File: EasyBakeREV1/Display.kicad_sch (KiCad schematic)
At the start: 20 parts, among them U4 SQ2310ES_SOT23, U5 NHD-C12832A1Z

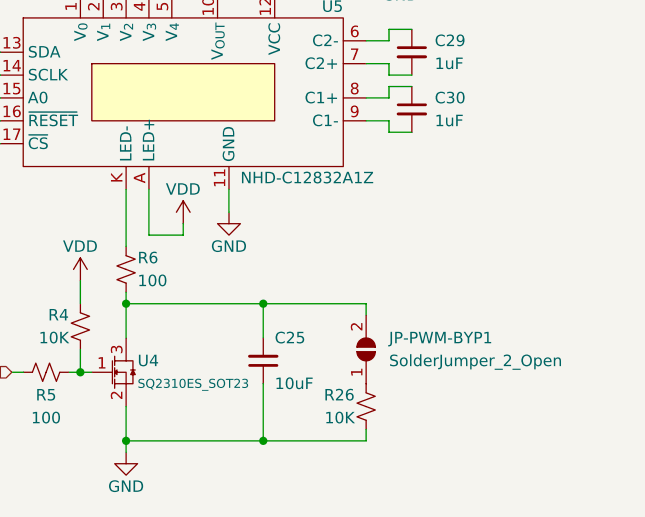
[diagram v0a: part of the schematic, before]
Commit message: REV3 - Reorganize MC pinouts and add LED driver (WIP)
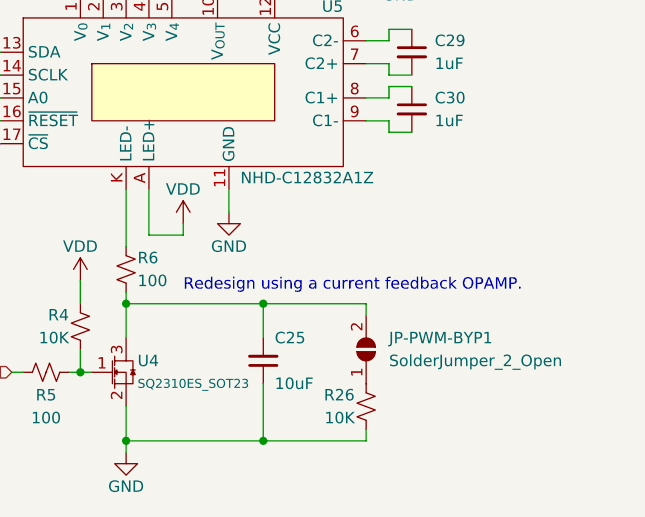
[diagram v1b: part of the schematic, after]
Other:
- note added: "Redesign using a current feedback OPAMP."
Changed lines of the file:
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@@
+    (effects (font (size 1.27 1.27)) (justify left bottom))
+  )
+  (text "Redesign using a current feedback OPAMP." (at 147.32 96.52 0)
     (effects (font (size 1.27 1.27)) (justify left bottom))
   )
@@
       (effects (font (size 1.27 1.27)) hide)
     )
-    (property "Datasheet" "C:\\Users\\Daxxn\\Documents\\Electrical\\Datasheets\\NHD-C12832A1Z.pdf" (id 3) (at 147.32 52.07 0)
+    (property "Datasheet" "%LOCAL_DATASHEETS%\\NHD-C12832A1Z.pdf" (id 3) (at 147.32 52.07 0)
       (effects (font (size 1.27 1.27)) hide)
     )

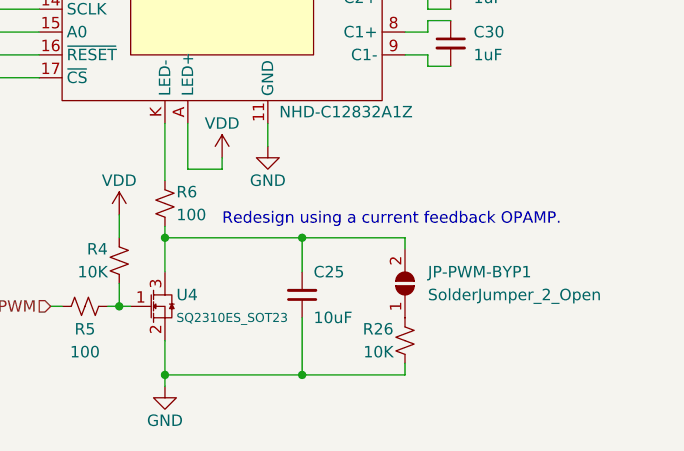
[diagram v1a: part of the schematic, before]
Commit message: Update to KiCad 7
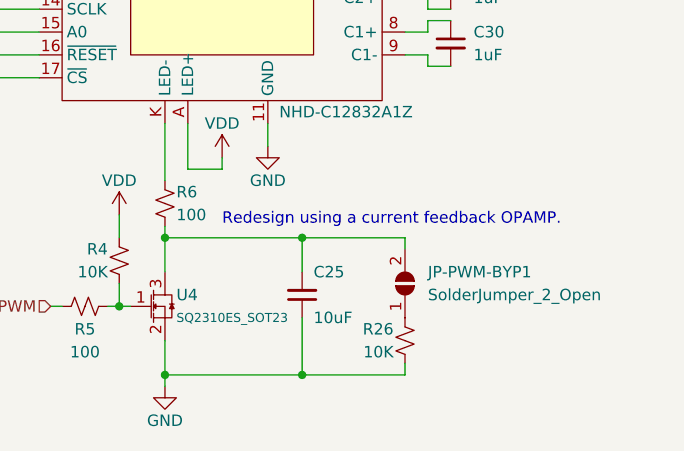
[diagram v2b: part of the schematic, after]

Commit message: Change main pwr to 3.3 due to USB issues
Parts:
- removed JP-PWM-BYP1: SolderJumper_2_Open, Jumper:SolderJumper-2_P1.3mm_Open_TrianglePad1.0x1.5mm, symbol Jumper:SolderJumper_2_Open
- removed R26: 10K, Resistor_SMD:R_0603_1608Metric, symbol Device:R_Small_US
- added Q1, Q2, Q3: MMBT2222A, Package_TO_SOT_SMD:SOT-23, symbol Daxxn_Transistors:MMBT2222A
- added R29, R30, R31, R35, R36, R37: 10K, Resistor_SMD:R_0603_1608Metric, symbol Device:R_Small_US
- added R32, R33, R34: 1K, Resistor_SMD:R_0603_1608Metric, symbol Device:R_Small_US
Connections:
- net DISP-A0: now also R32.2; no longer U5.15 (A0)
- net DISP-~{CS}: now also R34.2; no longer R3.2, U5.17 (~{CS})
- net DISP-~{RESET}: now also R33.1; no longer R2.2, U5.16 (~{RESET})
- net GND: now also Q1.1 (E), Q2.1 (E), Q3.1 (E), R36.2, R37.2
- net VDD: now also R29.1, R30.1, R31.1, R35.1; no longer R4.1
- new net: Q2.2 (B), R33.2, R35.2
- new net: Q1.2 (B), R32.1, R36.1
- new net: Q3.2 (B), R34.1, R37.1
- new net DISP-A0-B: Q1.3 (C), R29.2, U5.15 (A0)
- new net DISP-~{CS}-B: Q3.3 (C), R3.2, R31.2, U5.17 (~{CS})
- new net DISP-~{RESET}-B: Q2.3 (C), R2.2, R30.2, U5.16 (~{RESET})
- new net VCC: R4.1
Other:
- note removed: "Redesign using a current feedback OPAMP."
- moved on the sheet: C20, C21, C22, C23, C24, C25, C26, C27, C28, C29, C30, R2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

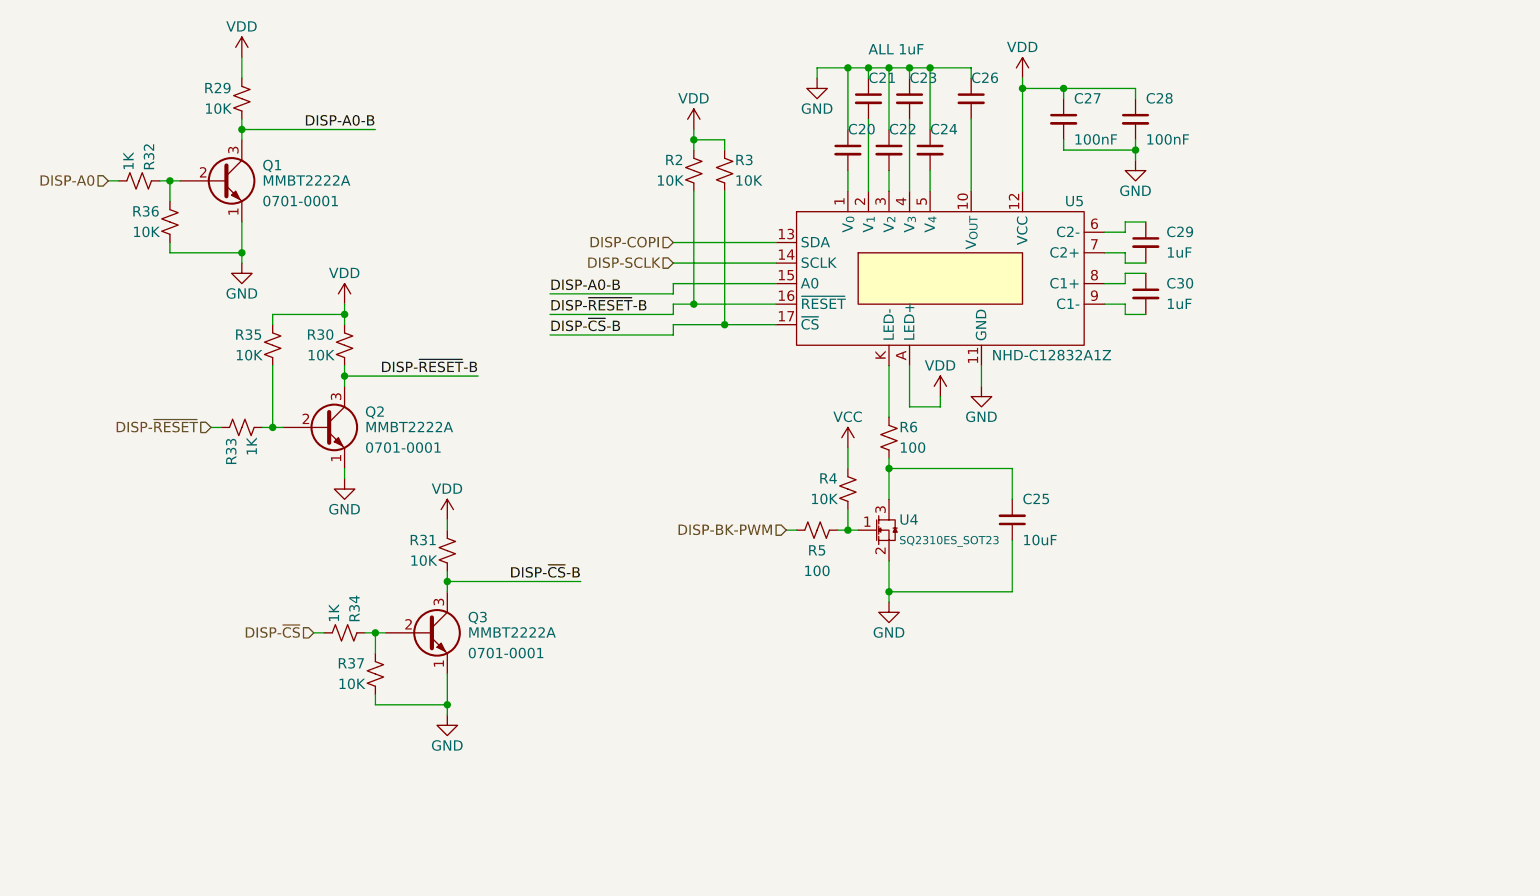
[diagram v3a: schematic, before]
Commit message: Replaced MCU - started layout
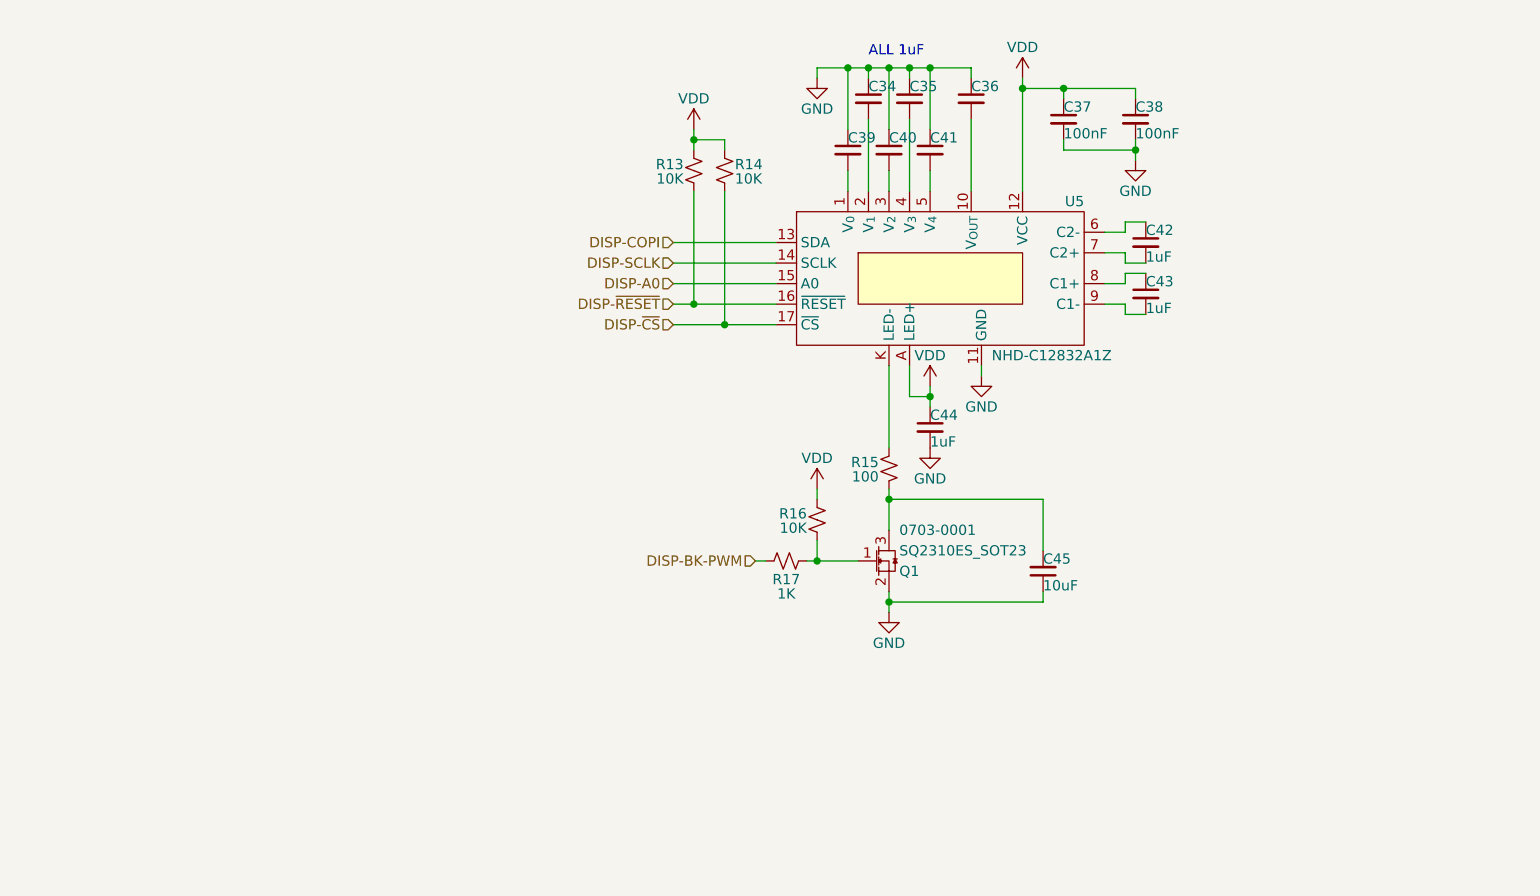
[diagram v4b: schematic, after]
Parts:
- removed Q1, Q2, Q3: MMBT2222A, Package_TO_SOT_SMD:SOT-23, symbol Daxxn_Transistors:MMBT2222A
- removed R29, R30, R31, R35, R36, R37: 10K, Resistor_SMD:R_0603_1608Metric, symbol Device:R_Small_US
- removed R32, R33, R34: 1K, Resistor_SMD:R_0603_1608Metric, symbol Device:R_Small_US
- removed U4: SQ2310ES_SOT23, Package_TO_SOT_SMD:SOT-23, symbol Daxxn_Transistors:SQ2310ES_SOT23
- added C44: 1uF, Capacitor_SMD:C_0805_2012Metric, symbol Device:C_Small
- added Q1: SQ2310ES_SOT23, Package_TO_SOT_SMD:SOT-23, symbol Daxxn_Transistors:SQ2310ES_SOT23
- C34: renamed from C21; footprint Capacitor_SMD:C_1210_3225Metric -> Capacitor_SMD:C_0805_2012Metric
- C35: renamed from C23; footprint Capacitor_SMD:C_1210_3225Metric -> Capacitor_SMD:C_0805_2012Metric
- C36: renamed from C26; footprint Capacitor_SMD:C_1210_3225Metric -> Capacitor_SMD:C_0805_2012Metric
- C37: renamed from C27; footprint Capacitor_SMD:C_0805_2012Metric -> Capacitor_SMD:C_0402_1005Metric
- C38: renamed from C28; footprint Capacitor_SMD:C_0805_2012Metric -> Capacitor_SMD:C_0402_1005Metric
- C39: renamed from C20; footprint Capacitor_SMD:C_1210_3225Metric -> Capacitor_SMD:C_0805_2012Metric
- C40: renamed from C22; footprint Capacitor_SMD:C_1210_3225Metric -> Capacitor_SMD:C_0805_2012Metric
- C41: renamed from C24; footprint Capacitor_SMD:C_1210_3225Metric -> Capacitor_SMD:C_0805_2012Metric
- C42: renamed from C29; footprint Capacitor_SMD:C_1210_3225Metric -> Capacitor_SMD:C_0805_2012Metric
- C43: renamed from C30; footprint Capacitor_SMD:C_1210_3225Metric -> Capacitor_SMD:C_0805_2012Metric
- C45: renamed from C25; footprint Capacitor_SMD:C_0805_2012Metric -> Capacitor_SMD:C_1210_3225Metric
- R13: renamed from R2; footprint Resistor_SMD:R_0603_1608Metric -> Resistor_SMD:R_0402_1005Metric
- R14: renamed from R3; footprint Resistor_SMD:R_0603_1608Metric -> Resistor_SMD:R_0402_1005Metric
- R15: renamed from R6; footprint Resistor_SMD:R_0603_1608Metric -> Resistor_SMD:R_0402_1005Metric
- R16: renamed from R4; footprint Resistor_SMD:R_0603_1608Metric -> Resistor_SMD:R_0402_1005Metric
- R17: renamed from R5; value 100 -> 1K; footprint Resistor_SMD:R_0603_1608Metric -> Resistor_SMD:R_0402_1005Metric
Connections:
- net DISP-A0-B is gone; now on net DISP-A0: U5.15 (A0)
- net DISP-~{CS}-B is gone; now on net DISP-~{CS}: R14.2, U5.17 (~{CS})
- net DISP-~{RESET}-B is gone; now on net DISP-~{RESET}: R13.2, U5.16 (~{RESET})
- net VCC is gone; now on net VDD: R16.1
- net GND: now also C44.2, Q1.2 (S)
- net VDD: now also C44.1
- net at R16.2, R17.1: now also Q1.1 (G)
- net at C45.2, R15.2: now also Q1.3 (D)
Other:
- moved on the sheet: C45, R15, R16, R17

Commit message: Rearrange footprints and start layout
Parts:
- C42, C43: value 1uF -> 2.2uF
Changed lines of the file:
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@@
       (effects (font (size 1.27 1.27)) (justify left))
     )
-    (property "Value" "1uF" (at 149.86 42.418 0)
+    (property "Value" "2.2uF" (at 149.86 42.418 0)
       (effects (font (size 1.27 1.27)) (justify left))
     )
@@
       (effects (font (size 1.27 1.27)) (justify left))
     )
-    (property "Value" "1uF" (at 149.86 48.768 0)
-      (effects (font (size 1.27 1.27)) (justify left))
-    )
+    (property "Value" "2.2uF" (at 149.86 48.768 0)
+      (effects (font (size 1.27 1.27)) (justify left))
+    )
